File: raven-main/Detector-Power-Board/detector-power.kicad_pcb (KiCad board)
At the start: 2 copper layers, 37 x 52.5 mm, 38 parts, among them J1 DeployLipo, J2 Conn_01x04, J9 UCLipo, U1 LT8330IS6-TRMPBF, U2 TPS22810DRV, U3 LM317LCLPRE3, U4 LM317LCLPRE3

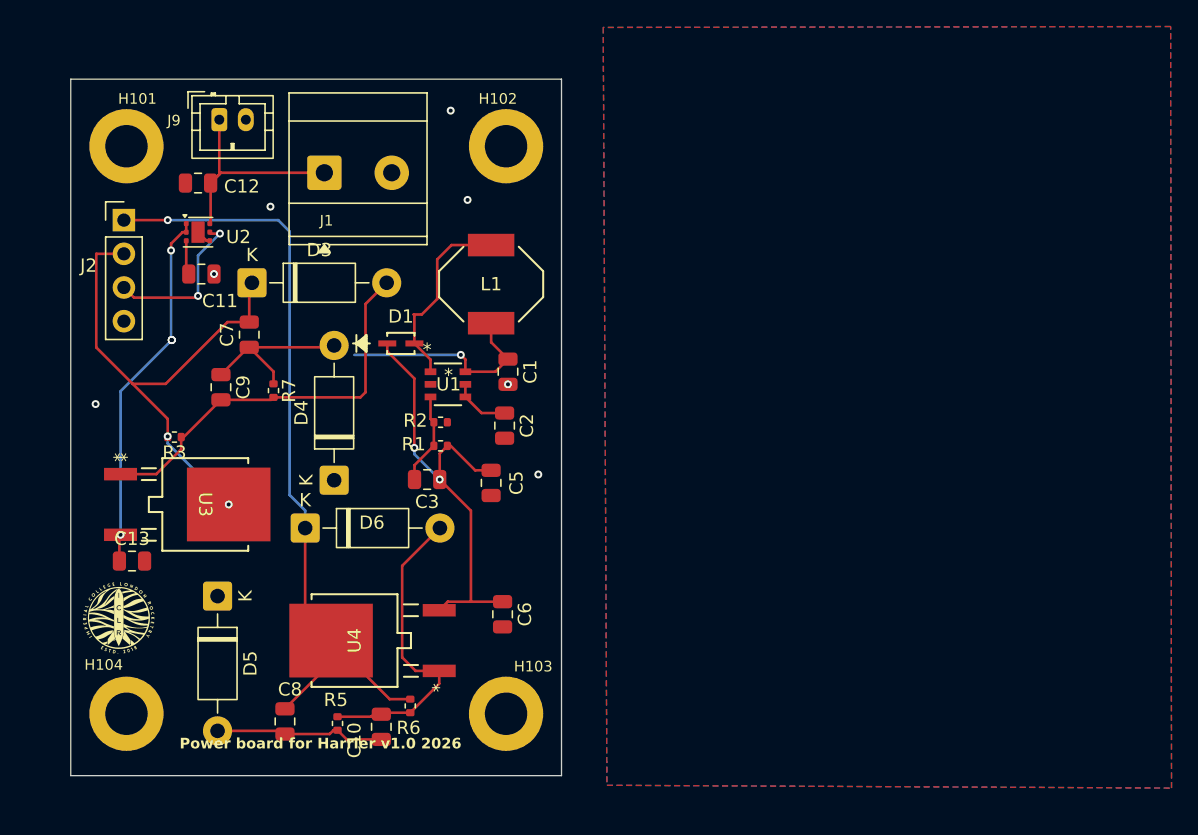
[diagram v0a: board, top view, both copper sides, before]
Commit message: More efficient routing
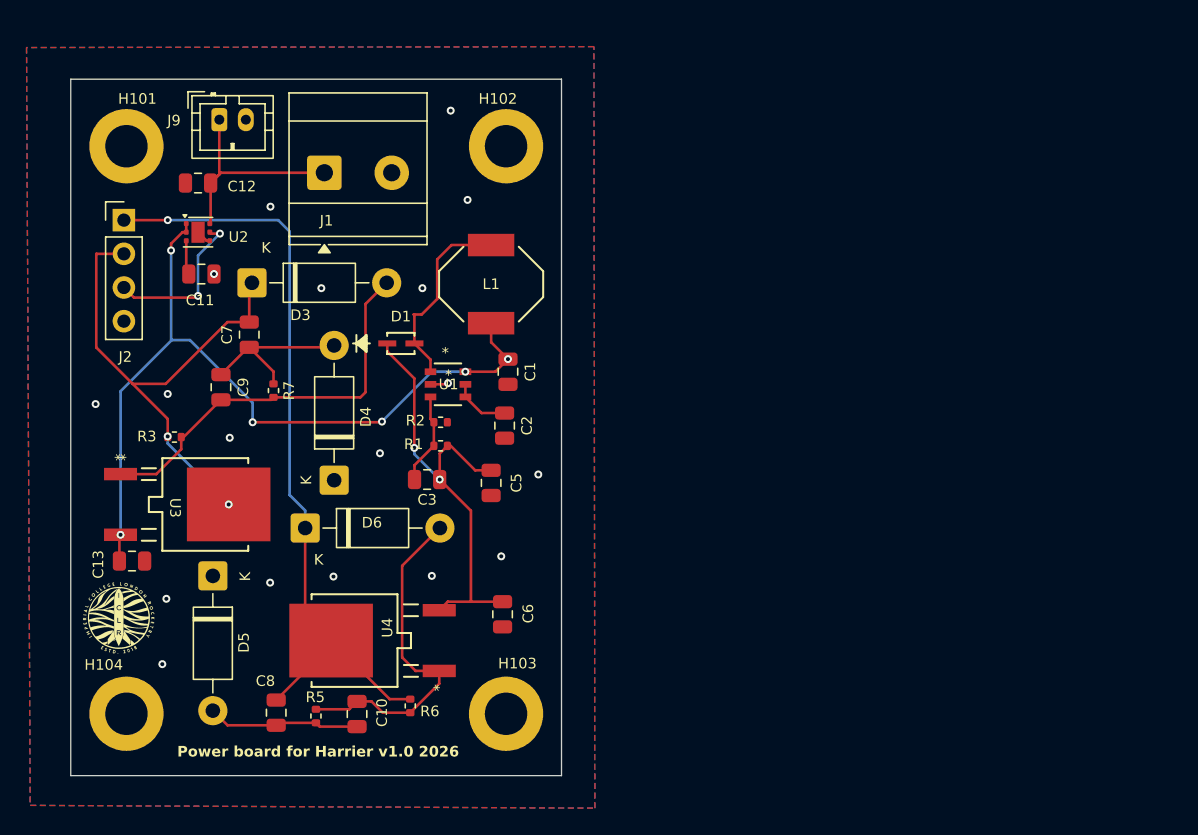
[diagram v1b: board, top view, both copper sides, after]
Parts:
- moved G*** 18.2 mm to (121.2, 84.8)
- moved G*** 3.25 mm to (139.3, 83.7)
- moved C10 2.07 mm to (132.4, 105.3)
- moved R5 1.72 mm to (129.3, 105.5)
- moved D5 1.56 mm to (121.5, 94.9)
- moved C8 0.93 mm to (126.3, 105.2)
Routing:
- net /BBIN: track 44.0 -> 61.9 mm
- net Net-(D6-A): track 23.8 -> 25.9 mm
- net GND: track 0.00 -> 1.36 mm, vias 7 -> 18
- net Net-(D5-A): track 12.8 -> 11.5 mm
- net /Filtered_Power_Out_25V: track 59.4 -> 60.6 mm
- net /Power_Out_5V: vias 3 -> 2

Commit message: power board done
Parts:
- removed C12: 5u, Capacitor_SMD:C_0805_2012Metric
- removed C13: 0.1u, Capacitor_SMD:C_0805_2012Metric
- removed D3, D4, D5, D6: 1N4002, Diode_THT:D_DO-41_SOD81_P10.16mm_Horizontal
- removed the G*** at (139.3, 83.7)
- removed J9: UCLipo, Connector_JST:JST_PH_B2B-PH-K_1x02_P2.00mm_Vertical
- removed the U3 at (120.9, 89.5)
- added C4: 4.7pF 50V, Capacitor_SMD:C_0402_1005Metric, F.Cu at (126.3, 87.6)
- added G***: LOGO, LOGO, B.Cu at (127.0, 84.0)
- added J3: Conn_01x03_Pin, Connector_Molex:Molex_Nano-Fit_105313-xx03_1x03_P2.50mm_Horizontal, F.Cu at (136.8, 81.5)
- added L2: 2.2uH, Inductor_SMD:L_0805_2012Metric, F.Cu at (134.0, 83.4)
- added R4: 10k, Resistor_SMD:R_0402_1005Metric, F.Cu at (127.1, 86.1)
- added U4: TPS62150, Package_DFN_QFN:VQFN-16-1EP_3x3mm_P0.5mm_EP1.68x1.68mm_ThermalVias, F.Cu at (130.9, 82.1)
- C1: value 4.7u -> 4.7uF 50V; footprint Capacitor_SMD:C_0805_2012Metric -> Capacitor_SMD:C_0603_1608Metric
- C10, C9: value 1u -> 10uF
- C11: value 1n -> 620pF; footprint Capacitor_SMD:C_0805_2012Metric -> Capacitor_SMD:C_0402_1005Metric
- C2, C8: value 1u -> 4.7uF; footprint Capacitor_SMD:C_0805_2012Metric -> Capacitor_SMD:C_0603_1608Metric
- C3: value 4.7p -> 4.7uF 50V; footprint Capacitor_SMD:C_0805_2012Metric -> Capacitor_SMD:C_0603_1608Metric
- C5: value 4.7u -> 100nF 50V; footprint Capacitor_SMD:C_0805_2012Metric -> Capacitor_SMD:C_0402_1005Metric
- C6: value 0.1u -> 1uF 50V; footprint Capacitor_SMD:C_0805_2012Metric -> Capacitor_SMD:C_0603_1608Metric
- C7: value 1u -> 1uF; footprint Capacitor_SMD:C_0805_2012Metric -> Capacitor_SMD:C_0603_1608Metric
- D1: value D_Schottky -> PMEG6010CEJ; footprint PMEG4010BEA:SOD323F_NEX -> Diode_SMD:D_SOD-323F
- J1: value DeployLipo -> Conn_01x02_Pin; footprint TerminalBlock_Phoenix:TerminalBlock_Phoenix_MKDS-3-2-5.08_1x02_P5.08mm_Horizontal -> Connector_Molex:Molex_Nano-Fit_105313-xx02_1x02_P2.50mm_Horizontal
- J2: value Conn_01x04 -> DeployLipo; footprint Connector_PinHeader_2.54mm:PinHeader_1x04_P2.54mm_Vertical -> Connector_AMASS:AMASS_XT60PW-M_1x02_P7.20mm_Horizontal
- L1: value 8.2u -> 6.8uH; footprint CDR7D28MNNP-8R0NC:IND_8R0NC_SUM -> iclr:WE-HEPC_6030
- R2: value 10k -> 240Ω
- R3: value 240 -> 4.56kΩ
- R5: value 4.56k -> 100k
- R6: value 240 -> 953k
- R7: value 720 -> 180k
- U2: renamed from U4; value LM317LCLPRE3 -> LM317LIDR; footprint LM317MDT_TR:DPAK_STM -> iclr:SOIC127P599X175-8N
- moved G*** 40.8 mm to (138.6, 65.1)
- moved L1 26.2 mm to (119.1, 84.6), turned to 0 degrees
- moved R6 26.0 mm to (132.9, 78.9)
- moved C8 24.8 mm to (127.2, 80.4), turned to 0 degrees
- moved R5 24.8 mm to (134.0, 81.1), turned to 180 degrees
- moved C10 20.0 mm to (130.7, 85.3), turned to 180 degrees
- moved C2 19.6 mm to (124.2, 80.4), turned to 180 degrees
- moved C1 19.2 mm to (124.6, 77.8), turned to 180 degrees
- moved G*** 17.7 mm to (125.0, 67.5)
- moved D1 16.3 mm to (123.6, 88.3), turned to 90 degrees
- moved R2 15.5 mm to (126.0, 92.2), turned to 180 degrees
- moved U3 15.5 mm to (124.3, 84.6), turned to 90 degrees
- moved C5 14.6 mm to (127.9, 87.8), turned to 0 degrees
- moved R1 13.6 mm to (125.3, 87.6), turned to 90 degrees
- moved H3 13.3 mm to (144.0, 92.0)
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- renumbered H101 to H1, H102 to H2, H103 to H3, H104 to H4, U2 to U1, U1 to U3
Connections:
- C1 pad 1: /BBIN -> /BATT+
- C10 pad 1: Net-(D5-A) -> /Power_Out_5V
- C10 pad 2: Net-(D6-A) -> GND
- C11 pad 1: Net-(U2-CT) -> Net-(U4-SS/TR)
- C2 pad 1: Net-(U1-EN/UVLO) -> /BBIN
- C3 pad 2: Net-(U1-FBX) -> GND
- C6 pad 1: /Power_Out_27.5V -> /Filtered_Power_Out_25V
- C7 pad 1: Net-(D4-A) -> Net-(U3-INTVCC)
- C7 pad 2: /Power_Out_5V -> GND
- C8 pad 1: Net-(D5-A) -> /BBIN
- C8 pad 2: /Filtered_Power_Out_25V -> GND
- C9 pad 1: Net-(D4-A) -> /Power_Out_5V
- C9 pad 2: Net-(D3-A) -> GND
- J1 pad 1: Net-(J1-Pin_1) -> GND
- J1 pad 2: GND -> /ON-OFF
- J2 pad 1: /Filtered_Power_Out_25V -> GND
- J2 pad 2: /Power_Out_5V -> /BATT+
- R1 pad 2: Net-(U1-FBX) -> Net-(U3-FBX)
- R2 pad 1: Net-(U1-FBX) -> /Filtered_Power_Out_25V
- R2 pad 2: GND -> Net-(U2-ADJUST)
- R3 pad 1: Net-(D3-A) -> Net-(U2-ADJUST)
- R3 pad 2: /Power_Out_5V -> GND
- R5 pad 1: Net-(D6-A) -> /Power_Out_5V
- R5 pad 2: Net-(D5-A) -> Net-(U4-PG)
- R6 pad 1: /Filtered_Power_Out_25V -> /Power_Out_5V
- R6 pad 2: Net-(D6-A) -> Net-(U4-FB)
- R7 pad 1: Net-(D4-A) -> Net-(U4-FB)
- R7 pad 2: Net-(D3-A) -> GND
- U1 pad 3: Net-(U2-CT) -> unconnected-(U1-CT-Pad3)
- U1 pad 4: Net-(U2-GND-Pad4) -> GND
- U1 pad 6: Net-(J1-Pin_1) -> /BATT+
- U1 pad 7: Net-(U2-GND-Pad4) -> GND
- U2 pad 1: Net-(D6-A) -> /Power_Out_27.5V
- U2 pad 2: /Power_Out_27.5V -> /Filtered_Power_Out_25V
- U3 pad 3: Net-(U1-FBX) -> Net-(U3-FBX)
- U3 pad 4: Net-(U1-EN/UVLO) -> /BBIN
- U3 pad 5: Net-(U1-EN/UVLO) -> Net-(U3-INTVCC)
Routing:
- net /BBIN: track 61.9 -> 17.8 mm, vias 6 -> 0
- net /Filtered_Power_Out_25V: track 60.6 -> 18.9 mm, vias 1 -> 0
- net /Power_Out_27.5V: track 34.2 -> 0.00 mm, vias 2 -> 0
- net Net-(D3-A): track 30.5 -> 0.00 mm
- net Net-(D6-A): track 25.9 -> 0.00 mm
- net Net-(J1-Pin_1): track 17.0 -> 0.00 mm
- net Net-(D1-A): track 14.6 -> 0.00 mm
- net Net-(D4-A): track 13.0 -> 0.00 mm
- net Net-(D5-A): track 11.5 -> 0.00 mm
- net /BATT+: track 0.00 -> 8.39 mm
- net Net-(U1-FBX): track 6.94 -> 0.00 mm
- net Net-(U1-EN/UVLO): track 4.41 -> 0.00 mm
- net Net-(U2-ADJUST): track 0.00 -> 4.16 mm
- net Net-(U3-INTVCC): track 0.00 -> 3.26 mm
- net Net-(L2-Pad1): track 0.00 -> 2.82 mm
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- added copper zone on F.Cu, net /BBIN
- added copper zone on F.Cu, net /Power_Out_27.5V
- added copper zone on F.Cu, net /Power_Out_5V
- added copper zone on F.Cu, net Net-(D1-A)
- added copper zone on F.Cu, net Net-(U3-FBX)
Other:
- board size 37 x 52.5 mm -> 35.5 x 37.5 mm
- board text added: "25V"
- board text added: "5V"
- board text added: "EN"
- board text added: "GND"
- board text added: "HARRIER-Zapdos v1.0"
- board text added: "HARRIER-Zapdos v1.0 2026"
- board text removed: "Power Board for HARRIER v1.0"
- board text removed: "Power board for Harrier v1.0 2026"

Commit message: updated detector - need to order
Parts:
- added G***: LOGO, Decor:harrier-draft, F.Cu at (126.9, 65.8)
- moved C10 2.57 mm to (133.1, 84.4)
- moved R5 1.80 mm to (134.1, 79.3)
- moved L2 1.80 mm to (134.0, 81.6)
- moved R6 1.31 mm to (133.6, 77.8), turned to 180 degrees
- moved C9 1.20 mm to (133.1, 86.4)
- moved R7 1.12 mm to (131.7, 77.8), turned to 180 degrees
- moved C11 1.10 mm to (129.2, 78.3)
- moved U4 1.10 mm to (130.9, 81.0)
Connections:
- J3 pad 1: GND -> /Power_Out_5V
- J3 pad 2: /Power_Out_5V -> GND
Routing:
- net /Power_Out_5V: track 41.4 -> 21.7 mm, vias 4 -> 2
- net Net-(L2-Pad1): track 2.82 -> 5.19 mm
- net Net-(U4-FB): track 2.33 -> 2.85 mm
- net /BBIN: track 17.8 -> 17.3 mm
- net GND: vias 0 -> 18
- removed copper zone on F.Cu, net /Power_Out_5V

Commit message: new docs/3d files
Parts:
- R1: value 162k -> 162kΩ
- R4: value 10k -> 10kΩ
- R5: value 100k -> 100kΩ
- R6: value 953k -> 953kΩ
- R7: value 180k -> 180kΩ
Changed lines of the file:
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@@
 			)
 		)
-		(property "Value" "953k"
+		(property "Value" "953kΩ"
 			(at 0 1.17 0)
 			(layer "F.Fab")
@@
 		)
 		(embedded_fonts no)
-		(model "${ICLR_HW}/3d/XT60PW MALE.STEP"
+		(model "/home/jak/Documents/iclr/iclr-hw/3d/XT60PW MALE.STEP"
 			(offset
 				(xyz 3.5 15.3 3.5)
@@
 		)
 		(embedded_fonts no)
+		(model "${KICAD10_3DMODEL_DIR}/Inductor_SMD.3dshapes/L_Cenker_CKCS6028.step"
+			(offset
+				(xyz 0 0 0)
+			)
+			(scale
+				(xyz 1 1 1)
+			)
+			(rotate
+				(xyz -0 -0 90)
+			)
+		)
 	)
 	(footprint "Resistor_SMD:R_0402_1005Metric"
@@
 			)
 		)
-		(property "Value" "100k"
+		(property "Value" "100kΩ"
 			(at 0 1.17 0)
 			(layer "F.Fab")
@@
 			)
 		)
-		(property "Value" "180k"
+		(property "Value" "180kΩ"
 			(at 0 1.17 0)
 			(layer "F.Fab")
@@
 			)
 		)
-		(property "Value" "162k"
+		(property "Value" "162kΩ"
 			(at 0 1.17 90)
 			(layer "F.Fab")
@@
 		)
 		(embedded_fonts no)
-		(model "${KICAD10_3DMODEL_DIR}/Connector_Molex.3dshapes/Molex_Nano-Fit_105313-xx03_1x03_P2.50mm_Horizontal.step"
+		(model "/home/jak/Documents/iclr/iclr-hw/3d/3pinnanofithorizontal.stp"
 			(offset
-				(xyz 0 0 0)
+				(xyz 6.25 -2.5 2)
 			)
 			(scale
@@
 			)
 			(rotate
-				(xyz 0 0 0)
+				(xyz -90 -0 -90)
 			)
 		)
@@
 		)
 		(embedded_fonts no)
-		(model "${KICAD10_3DMODEL_DIR}/Connector_Molex.3dshapes/Molex_Nano-Fit_105313-xx02_1x02_P2.50mm_Horizontal.step"
+		(model "/home/jak/Documents/iclr/iclr-hw/3d/2pinnanofithorizontal.STEP"
 			(offset
-				(xyz 0 0 0)
+				(xyz 6.25 -1.25 0)
 			)
 			(scale
@@
 			)
 			(rotate
-				(xyz 0 0 0)
+				(xyz -90 -0 -90)
 			)
 		)
@@
 			)
 		)
-		(property "Value" "10k"
+		(property "Value" "10kΩ"
 			(at 0 1.17 0)
 			(layer "F.Fab")
@@
 		)
 	)
-	(gr_text "GND"
-		(at 134.6 80.2 270)
+	(gr_text "5V"
+		(at 134.6 80.55 270)
 		(layer "F.SilkS")
 		(effects
@@
 		)
 	)
-	(gr_text "5V"
-		(at 134.6 83.2 270)
+	(gr_text "GND"
+		(at 134.6 82.7 270)
 		(layer "F.SilkS")
 		(effects
@@
 		)
 	)
-	(gr_text "25V"
-		(at 138.7 85.3 270)
+	(gr_text "GND"
+		(at 138.7 82.7 270)
 		(layer "F.SilkS")
 		(effects
@@
 		)
 	)
-	(gr_text "GND"
-		(at 138.8 80.2 270)
+	(gr_text "25V"
+		(at 138.7 85.3 270)
 		(layer "F.SilkS")
 		(effects
@@
 	)
 	(gr_text "5V"
-		(at 138.8 83.2 270)
+		(at 138.8 80.65 270)
 		(layer "F.SilkS")
 		(effects
